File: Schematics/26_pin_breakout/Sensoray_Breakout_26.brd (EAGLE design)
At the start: 54.3 x 30.5 mm, 14 parts, among them X1 87758-2616

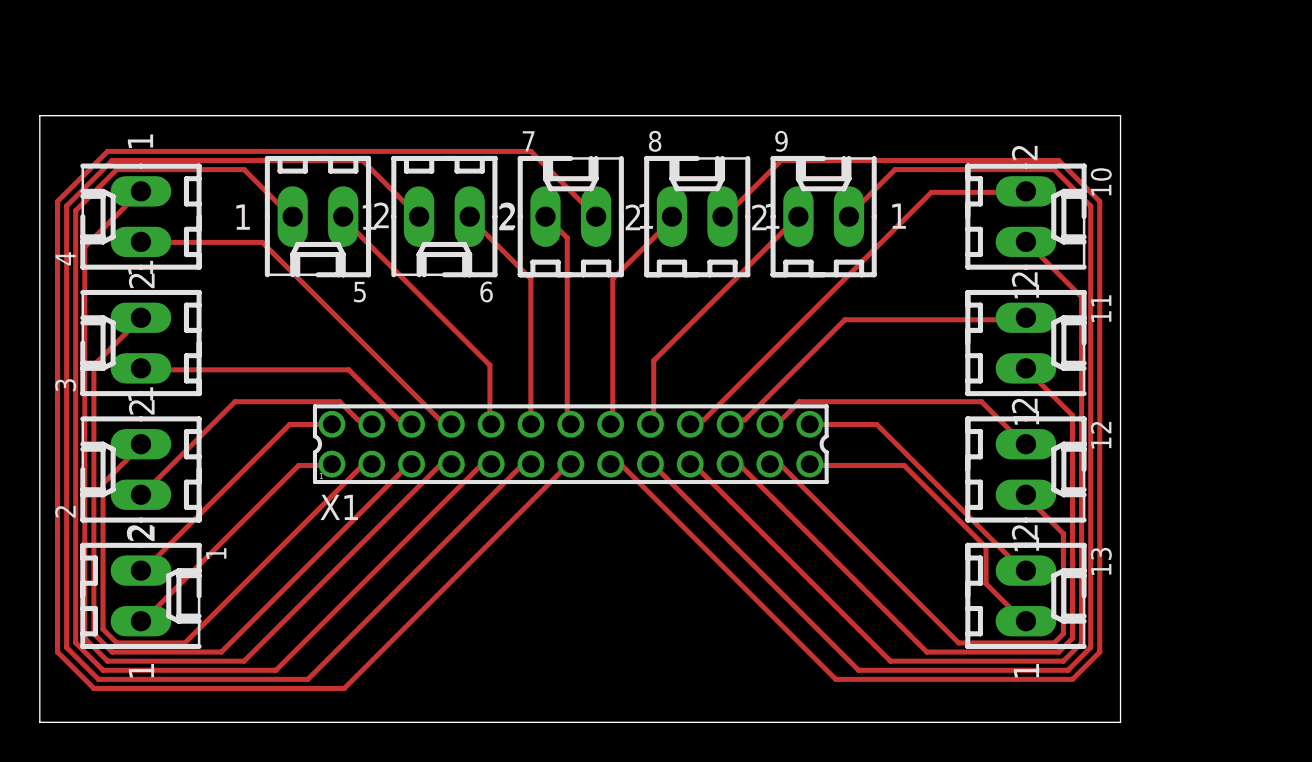
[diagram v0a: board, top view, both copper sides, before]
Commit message: added Rev 2 for 26 and 50 pin breakout boards, along with their gerber files for 1-layer PCB use. also added WPR for week of 27th
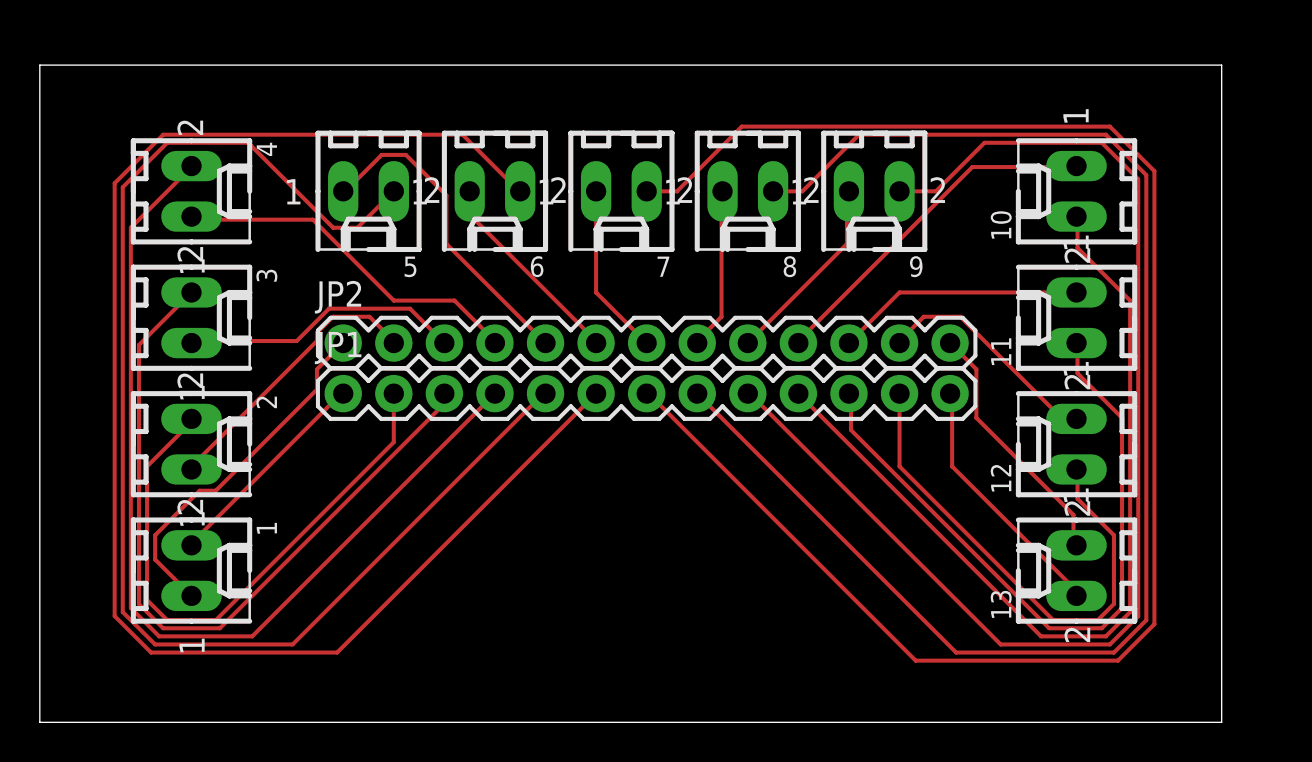
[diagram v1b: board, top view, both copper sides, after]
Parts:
- removed X1: 87758-2616, con-molex:87758-2616
- added JP1, JP2: M13, SparkFun-Connectors:1X13
- moved 5 2.84 mm to (16.5, 26.7)
- moved 4 2.84 mm to (7.62, 26.7), turned to 270 degrees
- moved 2 2.84 mm to (7.62, 14.0), turned to 270 degrees
- moved 1 2.84 mm to (7.62, 7.62)
- moved 10 2.84 mm to (52.1, 26.7), turned to 90 degrees
- moved 6 2.84 mm to (22.9, 26.7)
- moved 7 2.84 mm to (29.2, 26.7), turned to 180 degrees
- moved 8 2.84 mm to (35.6, 26.7), turned to 180 degrees
- moved 9 2.84 mm to (41.9, 26.7), turned to 180 degrees
- moved 12 2.84 mm to (52.1, 14.0), turned to 90 degrees
- moved 13 2.84 mm to (52.1, 7.62), turned to 90 degrees
- moved 3 2.84 mm to (7.62, 20.3), turned to 270 degrees
- moved 11 2.84 mm to (52.1, 20.3), turned to 90 degrees
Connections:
- net N$1: now also 1.2, JP1.1; no longer 1.1, X1.1
- net N$10: now also 10.2, JP1.10; no longer 9.1, X1.17
- net N$11: now also 11.2, JP1.11; no longer 10.1, X1.19
- net N$12: now also 12.2, JP1.12; no longer 11.1, X1.21
- net N$13: now also 13.2, JP1.13; no longer 12.1, X1.23
- net N$14: now also 1.1, JP2.1; no longer 13.1, X1.25
- net N$15: now also 2.1, JP2.2; no longer 2.2, X1.4
- net N$16: now also 3.1, JP2.3; no longer 3.2, X1.6
- net N$17: now also 4.1, JP2.4; no longer 4.2, X1.8
- net N$18: now also 5.1, JP2.5; no longer 5.2, X1.10
- net N$19: now also 6.1, JP2.6; no longer 6.2, X1.12
- net N$2: now also 2.2, JP1.2; no longer 1.2, X1.2
- net N$20: now also 7.1, JP2.7; no longer 7.2, X1.14
- net N$21: now also 13.1, JP2.13; no longer 8.2, X1.16
- net N$22: now also 12.1, JP2.12; no longer 9.2, X1.18
- net N$23: now also 11.1, JP2.11; no longer 10.2, X1.20
- net N$24: now also 10.1, JP2.10; no longer 11.2, X1.22
- net N$25: now also 9.1, JP2.9; no longer 12.2, X1.24
- net N$26: now also 8.1, JP2.8; no longer 13.2, X1.26
- net N$3: now also 3.2, JP1.3; no longer 2.1, X1.3
- net N$4: now also 4.2, JP1.4; no longer 3.1, X1.5
- net N$5: now also 5.2, JP1.5; no longer 4.1, X1.7
- net N$6: now also 6.2, JP1.6; no longer 5.1, X1.9
- net N$7: now also 7.2, JP1.7; no longer 6.1, X1.11
- net N$8: now also 8.2, JP1.8; no longer 7.1, X1.13
- net N$9: now also 9.2, JP1.9; no longer 8.1, X1.15
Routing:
- net N$10: track 62.9 -> 43.2 mm
- net N$5: track 46.6 -> 65.5 mm
- net N$2: track 12.6 -> 29.0 mm
- net N$6: track 60.2 -> 74.6 mm
- net N$13: track 26.4 -> 12.9 mm
- net N$9: track 73.2 -> 61.1 mm
- net N$7: track 70.5 -> 82.3 mm
- net N$8: track 83.3 -> 71.7 mm
- net N$11: track 45.4 -> 34.3 mm
- net N$12: track 35.9 -> 25.5 mm
- net N$4: track 37.1 -> 47.4 mm
- net N$3: track 27.6 -> 37.8 mm
- net N$23: track 21.7 -> 12.5 mm
- net N$26: track 13.9 -> 8.18 mm
- net N$25: track 14.2 -> 9.78 mm
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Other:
- board size 54.3 x 30.5 mm -> 59.4 x 33 mm

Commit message: final 26 pin layout
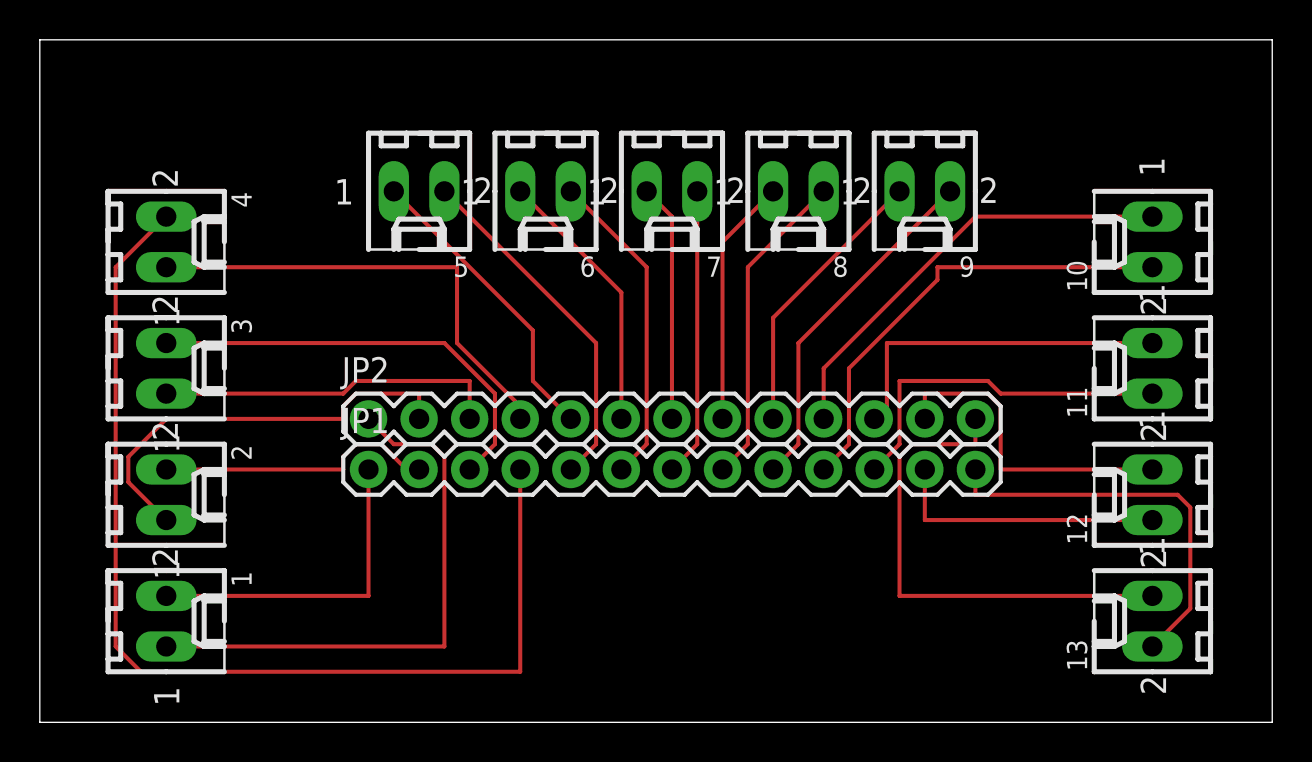
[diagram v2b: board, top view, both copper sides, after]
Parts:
- moved 10 4.58 mm to (55.9, 24.1)
- moved 11 4.58 mm to (55.9, 17.8)
- moved 12 4.58 mm to (55.9, 11.4)
- moved 13 4.58 mm to (55.9, 5.08)
- moved JP1 4.02 mm to (16.5, 12.7)
- moved JP2 4.02 mm to (16.5, 15.2)
- moved 4 2.84 mm to (6.35, 24.1)
- moved 2 2.84 mm to (6.35, 11.4)
- moved 1 2.84 mm to (6.35, 5.08)
- moved 3 2.84 mm to (6.35, 17.8)
- moved 9 2.54 mm to (44.5, 26.7)
- moved 5 2.54 mm to (19.1, 26.7)
- moved 6 2.54 mm to (25.4, 26.7)
- moved 7 2.54 mm to (31.8, 26.7)
- moved 8 2.54 mm to (38.1, 26.7)
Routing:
- net N$7: track 82.3 -> 14.5 mm
- net N$6: track 74.6 -> 16.1 mm
- net N$8: track 71.7 -> 16.1 mm
- net N$5: track 65.5 -> 17.7 mm
- net N$9: track 61.1 -> 17.7 mm
- net N$10: track 43.2 -> 23.3 mm
- net N$11: track 34.3 -> 17.9 mm
- net N$3: track 37.8 -> 21.9 mm
- net N$2: track 29.0 -> 14.1 mm
- net N$21: track 12.8 -> 25.0 mm
- net N$12: track 25.5 -> 14.0 mm
- net N$14: track 17.8 -> 28.1 mm
- net N$15: track 14.3 -> 21.5 mm
- net N$13: track 12.9 -> 20.1 mm
- net N$4: track 47.4 -> 53.6 mm
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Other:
- board size 59.4 x 33 mm -> 61.9 x 34.3 mm
